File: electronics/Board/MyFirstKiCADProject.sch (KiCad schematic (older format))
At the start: 8 parts, among them SW1 SPST, U1 MIC29312

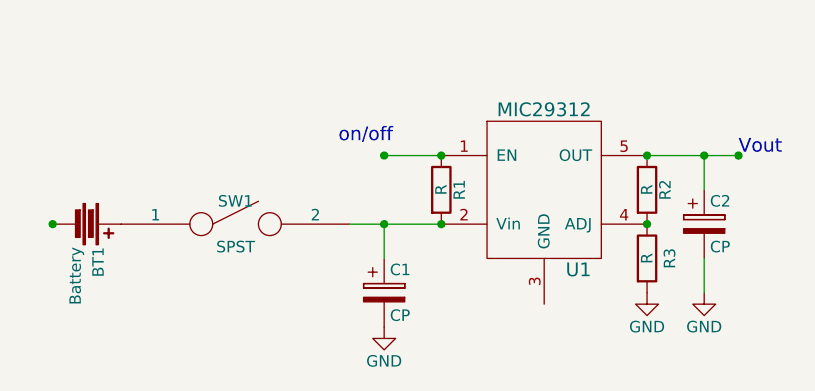
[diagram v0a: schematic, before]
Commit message: changed battery to connector, added R values, and grounds
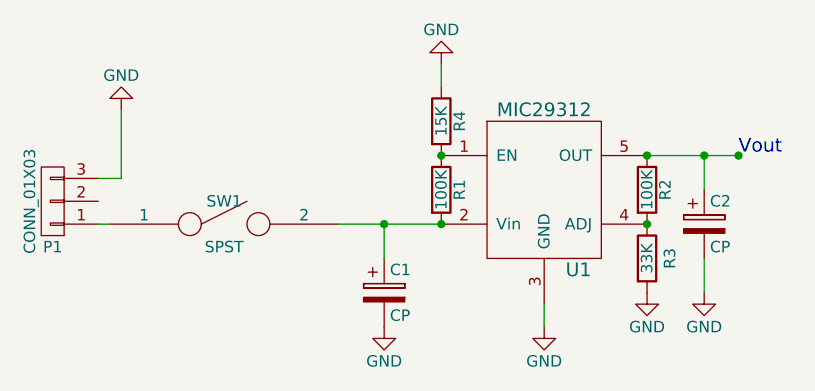
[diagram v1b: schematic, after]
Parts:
- removed BT1: Battery, symbol Battery
- added P1: CONN_01X03, symbol CONN_01X03
- added R4: 15K, symbol R
- R1, R2: value R -> 100K
- R3: value R -> 33K
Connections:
- net GND: now also U1.3 (GND), P1.3 (P3), R4.1
- net at R1.1, U1.1 (EN): now also R4.2
- net at SW1.1: now also P1.1 (P1)
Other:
- note removed: "on/off"
- moved on the sheet: SW1
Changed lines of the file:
@@
 P 6250 3400
 F 0 "R3" V 6350 3400 50  0000 C CNN
-F 1 "R" V 6250 3400 50  0000 C CNN
+F 1 "33K" V 6250 3400 50  0000 C CNN
 F 2 "" V 6180 3400 50  0000 C CNN
 F 3 "" H 6250 3400 50  0000 C CNN
@@
 P 6250 3100
 F 0 "R2" V 6330 3100 50  0000 C CNN
-F 1 "R" V 6250 3100 50  0000 C CNN
+F 1 "100K" V 6250 3100 50  0000 C CNN
 F 2 "" V 6180 3100 50  0000 C CNN
 F 3 "" H 6250 3100 50  0000 C CNN
@@
 $EndComp
 $Comp
-L GND #PWR2
+L GND #PWR5
 U 1 1 5754A5D9
 P 6250 3550
-F 0 "#PWR2" H 6250 3300 50  0001 C CNN
+F 0 "#PWR5" H 6250 3300 50  0001 C CNN
 F 1 "GND" H 6250 3400 50  0000 C CNN
 F 2 "" H 6250 3550 50  0000 C CNN
@@
 $EndComp
 $Comp
-L GND #PWR3
+L GND #PWR6
 U 1 1 5754A69C
 P 6500 3550
-F 0 "#PWR3" H 6500 3300 50  0001 C CNN
+F 0 "#PWR6" H 6500 3300 50  0001 C CNN
 F 1 "GND" H 6500 3400 50  0000 C CNN
 F 2 "" H 6500 3550 50  0000 C CNN
@@
 P 5350 3100
 F 0 "R1" V 5430 3100 50  0000 C CNN
-F 1 "R" V 5350 3100 50  0000 C CNN
+F 1 "100K" V 5350 3100 50  0000 C CNN
 F 2 "" V 5280 3100 50  0000 C CNN
 F 3 "" H 5350 3100 50  0000 C CNN
@@
 $EndComp
 Wire Wire Line
-	5350 2950 5100 2950
-Wire Wire Line
-	4950 3250 5350 3250
-Connection ~ 5100 2950
+	4900 3250 5350 3250
 Connection ~ 5100 3250
 Connection ~ 6250 2950
@@
 $EndComp
 $Comp
-L GND #PWR1
+L GND #PWR2
 U 1 1 5754A981
 P 5100 3700
-F 0 "#PWR1" H 5100 3450 50  0001 C CNN
+F 0 "#PWR2" H 5100 3450 50  0001 C CNN
 F 1 "GND" H 5100 3550 50  0000 C CNN
 F 2 "" H 5100 3700 50  0000 C CNN
@@
 L SPST SW1
 U 1 1 5754A9A1
-P 4450 3250
-F 0 "SW1" H 4450 3350 50  0000 C CNN
-F 1 "SPST" H 4450 3150 50  0000 C CNN
-F 2 "" H 4450 3250 50  0000 C CNN
-F 3 "" H 4450 3250 50  0000 C CNN
-	1    4450 3250
+P 4400 3250
+F 0 "SW1" H 4400 3350 50  0000 C CNN
+F 1 "SPST" H 4400 3150 50  0000 C CNN
+F 2 "" H 4400 3250 50  0000 C CNN
+F 3 "" H 4400 3250 50  0000 C CNN
+	1    4400 3250
 	1    0    0    -1
 $EndComp
 $Comp
-L Battery BT1
-U 1 1 5754A9DF
-P 3800 3250
-F 0 "BT1" H 3900 3300 50  0000 L CNN
-F 1 "Battery" H 3900 3200 50  0000 L CNN
-F 2 "" V 3800 3290 50  0000 C CNN
-F 3 "" V 3800 3290 50  0000 C CNN
-	1    3800 3250
-	0    1    1    0
+L CONN_01X03 P1
+U 1 1 5754C905
+P 3650 3150
+F 0 "P1" H 3650 3350 50  0000 C CNN
+F 1 "CONN_01X03" V 3750 3150 50  0000 C CNN
+F 2 "" H 3650 3150 50  0000 C CNN
+F 3 "" H 3650 3150 50  0000 C CNN
+	1    3650 3150
+	-1   0    0    1
 $EndComp
-Text Notes 4900 2900 0    60   ~ 0
-on/off
-Connection ~ 3650 3250
+Wire Wire Line
+	3900 3250 3850 3250
+Wire Wire Line
+	3850 3050 3950 3050
+Wire Wire Line
+	3950 3050 3950 2750
+$Comp
+L GND #PWR1
+U 1 1 5754CC86
+P 3950 2750
+F 0 "#PWR1" H 3950 2500 50  0001 C CNN
+F 1 "GND" H 3950 2600 50  0000 C CNN
+F 2 "" H 3950 2750 50  0000 C CNN
+F 3 "" H 3950 2750 50  0000 C CNN
+	1    3950 2750
+	-1   0    0    1
+$EndComp
+$Comp
+L R R4
+U 1 1 5754CD60
+P 5350 2800
+F 0 "R4" V 5430 2800 50  0000 C CNN
+F 1 "15K" V 5350 2800 50  0000 C CNN
+F 2 "" V 5280 2800 50  0000 C CNN
+F 3 "" H 5350 2800 50  0000 C CNN
+	1    5350 2800
+	1    0    0    -1
+$EndComp
+$Comp
+L GND #PWR3
+U 1 1 5754CDEF
+P 5350 2550
+F 0 "#PWR3" H 5350 2300 50  0001 C CNN
+F 1 "GND" H 5350 2400 50  0000 C CNN
+F 2 "" H 5350 2550 50  0000 C CNN
+F 3 "" H 5350 2550 50  0000 C CNN
+	1    5350 2550
+	-1   0    0    1
+$EndComp
+Wire Wire Line
+	5350 2650 5350 2550
+$Comp
+L GND #PWR4
+U 1 1 5754CF86
+P 5800 3700
+F 0 "#PWR4" H 5800 3450 50  0001 C CNN
+F 1 "GND" H 5800 3550 50  0000 C CNN
+F 2 "" H 5800 3700 50  0000 C CNN
+F 3 "" H 5800 3700 50  0000 C CNN
+	1    5800 3700
+	1    0    0    -1
+$EndComp
+Wire Wire Line
+	5800 3600 5800 3700
 $EndSCHEMATC
